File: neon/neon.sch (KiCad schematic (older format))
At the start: 10 parts

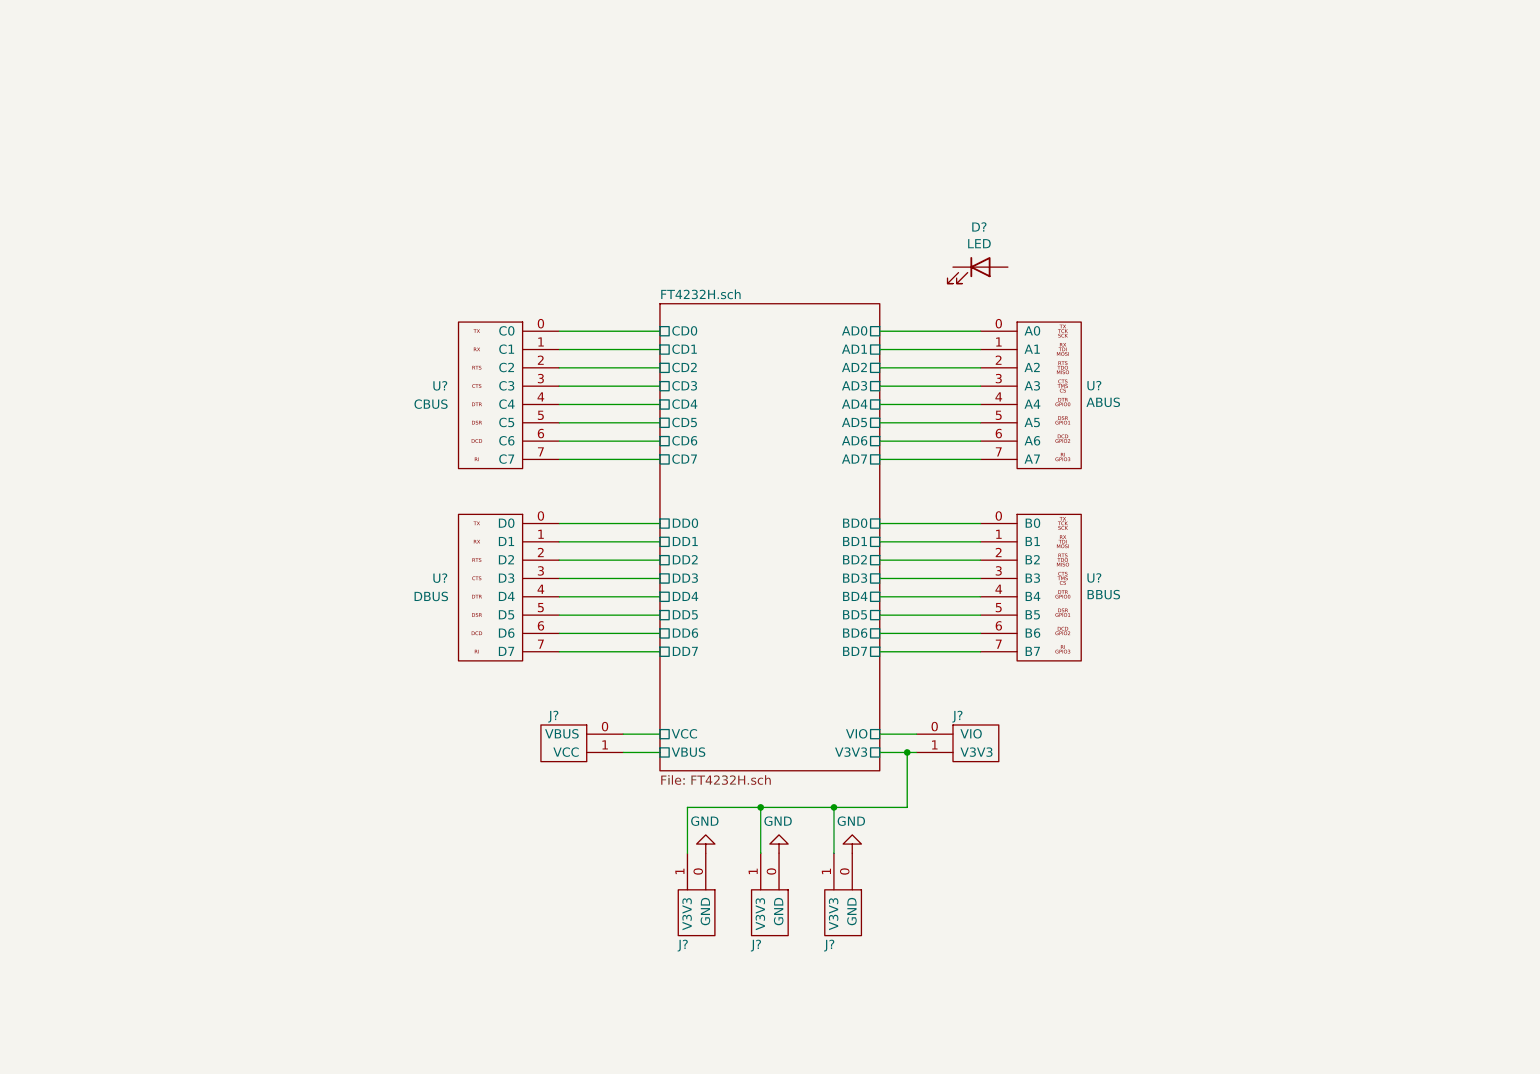
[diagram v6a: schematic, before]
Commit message: Add LEDs
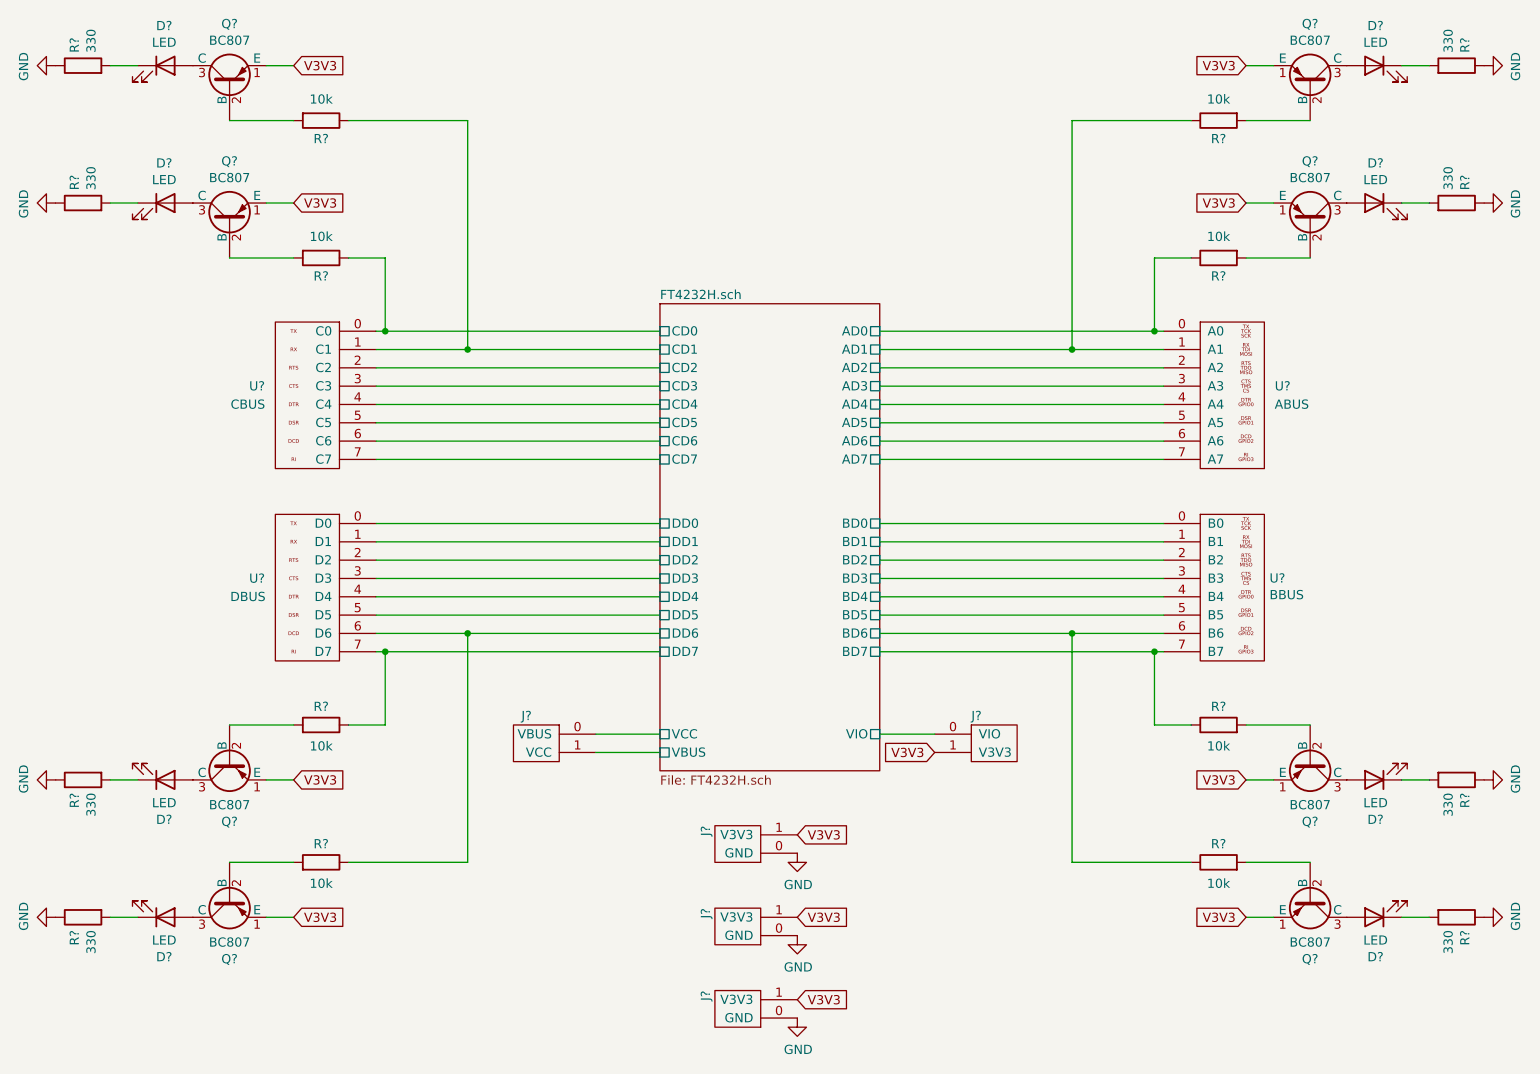
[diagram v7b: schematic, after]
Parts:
- removed D?: LED, symbol Device:LED
- removed J? (x2): V3V3-GND, symbol FTDI:V3V3-GND
- removed U?: ABUS, symbol FTDI:ABUS
- added D? (x8): LED, symbol Device:LED
- added J? (x2): V3V3-GND, symbol FTDI:V3V3-GND
- added Q? (x8): BC807, Package_TO_SOT_SMD:SOT-23, symbol FTDI_transistors:BC807
- added R? (x8): 330, symbol Device:R
- added R? (x8): 10k, symbol Device:R
- added U?: ABUS, symbol FTDI:ABUS
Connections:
- net FT4232H.sch/AD0: now also R?.1, U?.0 (A0)
- net FT4232H.sch/AD1: now also R?.1, U?.1 (A1)
- net FT4232H.sch/AD2: now also U?.2 (A2)
- net FT4232H.sch/AD3: now also U?.3 (A3)
- net FT4232H.sch/AD4: now also U?.4 (A4)
- net FT4232H.sch/AD5: now also U?.5 (A5)
- net FT4232H.sch/AD6: now also U?.6 (A6)
- net FT4232H.sch/AD7: now also U?.7 (A7)
- net FT4232H.sch/BD6: now also R?.1
- net FT4232H.sch/BD7: now also R?.1
- net FT4232H.sch/CD0: now also R?.1
- net FT4232H.sch/CD1: now also R?.1
- net FT4232H.sch/DD6: now also R?.1
- net FT4232H.sch/DD7: now also R?.1
- net GND: now also J?.0 (GND), J?.0 (GND), R?.1, R?.1, R?.1, R?.1, R?.1, R?.1, R?.1, R?.1
- net FT4232H.sch/V3V3 renamed V3V3
- net V3V3: now also J?.1 (V3V3), J?.1 (V3V3), Q?.1 (E), Q?.1 (E), Q?.1 (E), Q?.1 (E), Q?.1 (E), Q?.1 (E), Q?.1 (E), Q?.1 (E)
- new net: Q?.2 (B), R?.2 (x8)
- new net: D?.2 (A), Q?.3 (C) (x8)
- new net: D?.1 (K), R?.2 (x8)
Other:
- moved on the sheet: J?, U?

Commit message: Annotate components
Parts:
- removed R? (x7): 330, symbol Device:R
- added R1, R13, R14, R15, R2, R3, R4: 330, symbol Device:R
- gave numbers to parts that had none: 34
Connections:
- net GND: now also R1.2, R13.1, R14.1, R15.1, R2.2, R3.2, R4.2
- net at D1.1 (K): now also R1.1
- net at D2.1 (K): now also R2.1
- net at D5.1 (K): now also R13.2
- net at D6.1 (K): now also R14.2
- net at D7.1 (K): now also R15.2
- net at D3.1 (K): now also R3.1
- net at D4.1 (K): now also R4.1
